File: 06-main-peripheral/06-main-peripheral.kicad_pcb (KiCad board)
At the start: 4 copper layers, 58.5 x 29.2 mm, 17 parts, among them J1 T4040014041000, J2 FH-41-15S-0.5SH-05_, J3 T4040014041000, J4 T4040014041000, Q1 DMN3018SSD-13, SW1 100SP1K1B25M1QEH-ND, U1 LM74700-Q1

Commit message: before revision from overlords
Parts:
- C1, C3, C4, C5: footprint Capacitor_SMD:C_0402_1005Metric_Pad0.74x0.62mm_HandSolder -> Capacitor_SMD:C_0603_1608Metric_Pad1.08x0.95mm_HandSolder
- R1, R2: footprint Resistor_SMD:R_0402_1005Metric_Pad0.72x0.64mm_HandSolder -> Resistor_SMD:R_0603_1608Metric_Pad0.98x0.95mm_HandSolder
- moved R1 3.24 mm to (150.5, 85.0)
- moved C4 1.84 mm to (141.8, 77.5)
- moved C3 0.59 mm to (177.1, 83.4)
- moved Q1 0.56 mm to (172.4, 81.6)
- moved R2 0.53 mm to (138.7, 78.5)
- moved C1 0.47 mm to (186.0, 83.3)
- moved C5 0.45 mm to (152.6, 79.1)
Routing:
- net LED_CONTROL: track 9.06 -> 12.0 mm
- net TX_N: track 13.1 -> 11.1 mm
- net USB_D_N: track 19.3 -> 17.7 mm
- net RX_N: track 11.6 -> 10.1 mm
- net GND: track 18.9 -> 20.4 mm
- net 5V: track 4.74 -> 6.01 mm
- added copper zone on B.Cu, net GND
- added copper zone on F.Cu, net GND

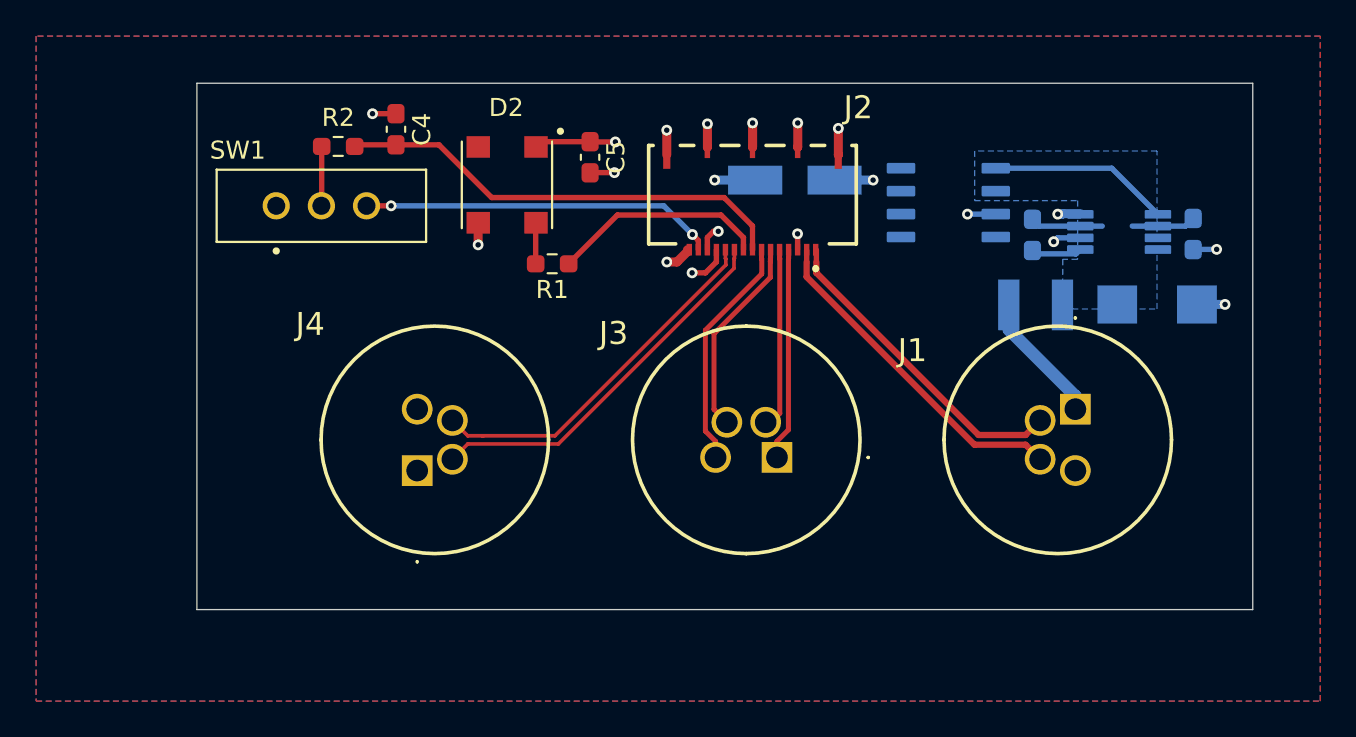
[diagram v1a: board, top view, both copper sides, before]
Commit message: added stitching vias
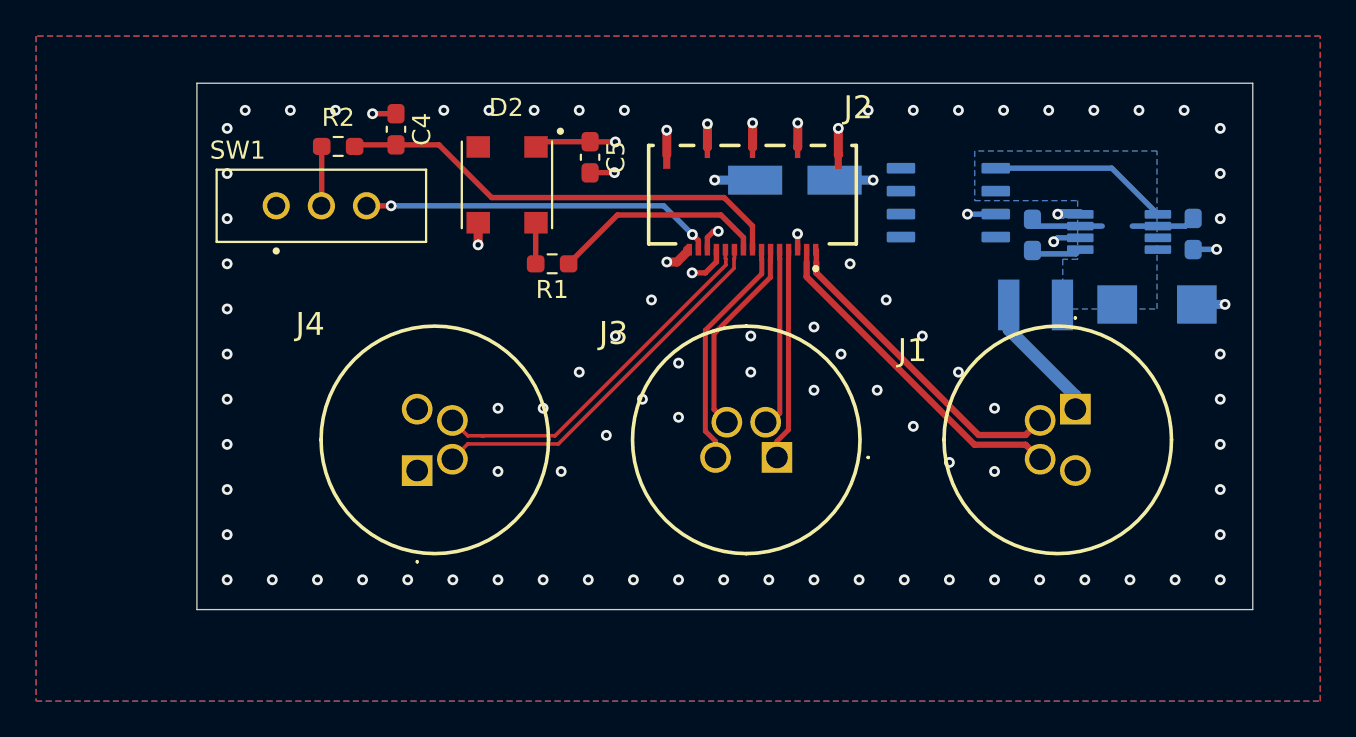
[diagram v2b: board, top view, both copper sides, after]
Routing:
- net GND: vias 14 -> 96

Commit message: added stitching vias correctly hopefully
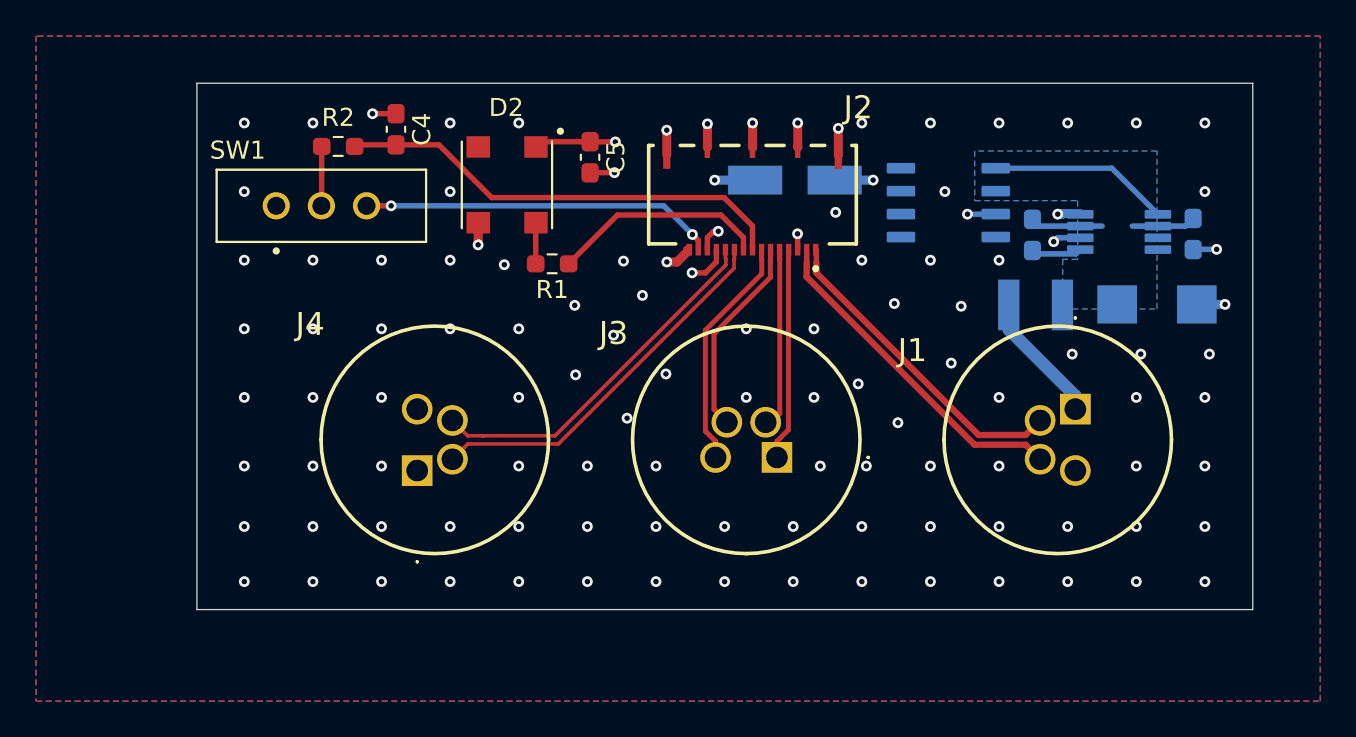
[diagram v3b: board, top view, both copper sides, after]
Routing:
- net GND: vias 96 -> 110

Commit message: fixed stitching vias
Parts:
- moved C2 0.21 mm to (164.2, 80.4)
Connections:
- J2 pad MP2: (no net) -> GND
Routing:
- net GND: vias 110 -> 108

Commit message: fixed stitching vias again
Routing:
- net GND: vias 108 -> 73

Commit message: Fixed mosfet routing
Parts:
- moved C2 0.25 mm to (163.9, 80.4), turned to 0 degrees
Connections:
- Q1 pad 1: Net-(Q1-G) -> Net-(D1-A2)
- Q1 pad 2: Net-(D1-A2) -> Net-(Q1-G)
- Q1 pad 3: USB_5V -> (no net)
- Q1 pad 7: (no net) -> USB_5V
- Q1 pad 8: (no net) -> USB_5V
- U1 pad 4: USB_5V -> GND
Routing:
- net Net-(Q1-G): track 9.48 -> 17.4 mm
- net USB_5V: track 6.39 -> 1.42 mm, vias 4 -> 3
- net GND: track 20.4 -> 21.7 mm, vias 73 -> 72
- added copper zone on B.Cu, net USB_5V
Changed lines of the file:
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@@
 		(capping no)
 		(filling no)
-		(zone_defaults)
 		(grid_origin 132.5 77.5)
 		(pcbplotparams
@@
 			(outputformat 1)
 			(mirror no)
-			(drillshape 1)
+			(drillshape 0)
 			(scaleselection 1)
 			(outputdirectory "")
@@
 	(footprint "Main_Peripheral:WCAP-ASLI_5X5.5_DXL_"
 		(layer "B.Cu")
-		(at 164.15 80.3656 180)
+		(at 163.9 80.3656)
 		(property "Reference" "C2"
 			(at -0.0086 3.7656 0)
@@
 		(duplicate_pad_numbers_are_jumpers no)
 		(fp_line
-			(start 2.75 1.7)
-			(end 2.75 1.1)
+			(start -2.75 -2.75)
+			(end -2.75 -1.1)
 			(stroke
 				(width 0.2)
@@
 		)
 		(fp_line
-			(start 2.75 -1.7)
-			(end 2.75 -1.1)
+			(start -2.75 -2.75)
+			(end 1.7 -2.75)
 			(stroke
 				(width 0.2)
@@
 		)
 		(fp_line
-			(start 1.7 2.75)
-			(end 2.75 1.7)
+			(start -2.75 2.75)
+			(end -2.75 1.1)
 			(stroke
 				(width 0.2)
@@
 		)
 		(fp_line
-			(start 1.7 -2.75)
-			(end 2.75 -1.7)
+			(start -2.75 2.75)
+			(end 1.7 2.75)
 			(stroke
 				(width 0.2)
@@
 		)
 		(fp_line
-			(start -2.75 2.75)
-			(end 1.7 2.75)
+			(start 1.7 -2.75)
+			(end 2.75 -1.7)
 			(stroke
 				(width 0.2)
@@
 		)
 		(fp_line
-			(start -2.75 2.75)
-			(end -2.75 1.1)
+			(start 1.7 2.75)
+			(end 2.75 1.7)
 			(stroke
 				(width 0.2)
@@
 		)
 		(fp_line
-			(start -2.75 -2.75)
-			(end 1.7 -2.75)
+			(start 2.75 -1.7)
+			(end 2.75 -1.1)
 			(stroke
 				(width 0.2)
@@
 		)
 		(fp_line
-			(start -2.75 -2.75)
-			(end -2.75 -1.1)
+			(start 2.75 1.7)
+			(end 2.75 1.1)
 			(stroke
 				(width 0.2)
@@
 		)
 		(fp_line
-			(start 2.65 1.65)
-			(end 1.65 2.65)
+			(start -2.65 -2.65)
+			(end 1.65 -2.65)
 			(stroke
 				(width 0.1)
@@
 		)
 		(fp_line
-			(start 2.65 -1.65)
-			(end 2.65 1.65)
+			(start -2.65 2.65)
+			(end -2.65 -2.65)
 			(stroke
 				(width 0.1)
@@
 		)
 		(fp_line
-			(start 1.65 2.65)
-			(end -2.65 2.65)
+			(start 1.65 -2.65)
+			(end 2.65 -1.65)
 			(stroke
 				(width 0.1)
@@
 		)
 		(fp_line
-			(start 1.65 -2.65)
-			(end 2.65 -1.65)
+			(start 1.65 2.65)
+			(end -2.65 2.65)
 			(stroke
 				(width 0.1)
@@
 		)
 		(fp_line
-			(start -2.65 2.65)
-			(end -2.65 -2.65)
+			(start 2.65 -1.65)
+			(end 2.65 1.65)
 			(stroke
 				(width 0.1)
@@
 		)
 		(fp_line
-			(start -2.65 -2.65)
-			(end 1.65 -2.65)
+			(start 2.65 1.65)
+			(end 1.65 2.65)
 			(stroke
 				(width 0.1)
@@
 		)
 		(pad "1" smd rect
-			(at 2.2 0 180)
+			(at 2.2 0)
 			(size 3 1.6)
 			(layers "B.Cu" "B.Mask" "B.Paste")
@@
 		)
 		(pad "2" smd rect
-			(at -2.2 0 180)
+			(at -2.2 0)
 			(size 3 1.6)
 			(layers "B.Cu" "B.Mask" "B.Paste")
@@
 			(unit
 				(name "A")
-				(pins "1" "3" "2")
+				(pins "2" "7" "1")
 			)
 		)
@@
 			(layers "B.Cu" "B.Mask" "B.Paste")
 			(roundrect_rratio 0.125)
-			(net "Net-(Q1-G)")
-			(pinfunction "G_1")
-			(pintype "input")
+			(net "Net-(D1-A2)")
+			(pinfunction "S_1")
+			(pintype "passive")
 			(solder_mask_margin 0.102)
 		)
@@
 			(layers "B.Cu" "B.Mask" "B.Paste")
 			(roundrect_rratio 0.125)
-			(net "Net-(D1-A2)")
-			(pinfunction "S_2")
-			(pintype "passive")
+			(net "Net-(Q1-G)")
+			(pinfunction "G_2")
+			(pintype "input")
 			(solder_mask_margin 0.102)
 		)
@@
 			(layers "B.Cu" "B.Mask" "B.Paste")
 			(roundrect_rratio 0.125)
-			(net "USB_5V")
-			(pinfunction "D_3")
-			(pintype "passive")
 			(solder_mask_margin 0.102)
 		)
@@
 			(layers "B.Cu" "B.Mask" "B.Paste")
 			(roundrect_rratio 0.125)
+			(net "USB_5V")
+			(pinfunction "D_7")
+			(pintype "passive")
 			(solder_mask_margin 0.102)
 		)
@@
 			(layers "B.Cu" "B.Mask" "B.Paste")
 			(roundrect_rratio 0.125)
+			(net "USB_5V")
 			(solder_mask_margin 0.102)
 		)
@@
 			(layers "B.Cu" "B.Mask" "B.Paste")
 			(roundrect_rratio 0.125)
-			(net "USB_5V")
+			(net "GND")
 			(pinfunction "CATHODE_4")
 			(pintype "input")
@@
 	)
 	(via
+		(at 159.8086 80.3656)
+		(size 0.6)
+		(drill 0.3)
+		(layers "F.Cu" "B.Cu")
+		(free yes)
+		(net "GND")
+	)
+	(via
 		(at 137.25 77.2)
 		(size 0.6)
@@
 	)
 	(via
-		(at 168.4836 80.3656)
-		(size 0.6)
-		(drill 0.3)
-		(layers "F.Cu" "B.Cu")
-		(net "GND")
-	)
-	(via
 		(at 156.25 102.6)
 		(size 0.6)
@@
 	)
 	(via
-		(at 166.2 82.15)
-		(size 0.6)
-		(drill 0.3)
-		(layers "F.Cu" "B.Cu")
-		(free yes)
-		(net "GND")
-	)
-	(via
 		(at 153.95 79.95)
 		(size 0.6)
@@
 	)
 	(via
-		(at 172.25 81)
-		(size 0.6)
-		(drill 0.3)
-		(layers "F.Cu" "B.Cu")
-		(free yes)
-		(net "GND")
-	)
-	(via
 		(at 141.05 88.6)
 		(size 0.6)
@@
 	)
 	(via
+		(at 178.5 82.25)
+		(size 0.6)
+		(drill 0.3)
+		(layers "F.Cu" "B.Cu")
+		(free yes)
+		(net "GND")
+	)
+	(via
 		(at 163.85 102.6)
 		(size 0.6)
@@
 	)
 	(segment
+		(start 159.8086 80.3656)
+		(end 161.95 80.3656)
+		(width 0.5)
+		(layer "B.Cu")
+		(net "GND")
+	)
+	(segment
 		(start 187.3 84.2)
 		(end 186.0125 84.2)
@@
 	)
 	(segment
+		(start 178.5 82.25)
+		(end 178.75 82.25)
+		(width 0.5)
+		(layer "B.Cu")
+		(net "GND")
+	)
+	(segment
 		(start 179.7431 83.567)
 		(end 179.7483 83.5618)
@@
 	)
 	(segment
-		(start 168.4836 80.3656)
-		(end 166.35 80.3656)
+		(start 178.75 82.25)
+		(end 178.7782 82.2218)
 		(width 0.5)
 		(layer "B.Cu")
@@
 	)
 	(segment
+		(start 178.7782 82.2218)
+		(end 179.7483 82.2218)
+		(width 0.5)
+		(layer "B.Cu")
+		(net "GND")
+	)
+	(segment
 		(start 146.606354 94.5235)
 		(end 146.706791 94.5235)
@@
 	)
 	(via
-		(at 159.8086 80.3656)
+		(at 168.35 79.9)
 		(size 0.6)
 		(drill 0.3)
@@
 	)
 	(via
-		(at 173.5 82.25)
+		(at 168.35 80.85)
 		(size 0.6)
 		(drill 0.3)
@@
 		(net "USB_5V")
 	)
-	(via
-		(at 178.5 82.25)
-		(size 0.6)
-		(drill 0.3)
-		(layers "F.Cu" "B.Cu")
-		(free yes)
-		(net "USB_5V")
-	)
 	(segment
-		(start 159.8086 80.3656)
-		(end 161.95 80.3656)
-		(width 0.5)
+		(start 173.7 79.1)
+		(end 173.7 80.5)
+		(width 0.3)
 		(layer "B.Cu")
-		(net "USB_5V")
+		(net "Net-(Q1-G)")
 	)
 	(segment
-		(start 175.0637 82.25)
-		(end 175.0675 82.2462)
+		(start 174.3 78.5)
+		(end 173.7 79.1)
 		(width 0.3)
 		(layer "B.Cu")
-		(net "USB_5V")
+		(net "Net-(Q1-G)")
 	)
 	(segment
-		(start 173.5 82.25)
-		(end 175.0637 82.25)
+		(start 184.3 82.0101)
+		(end 184.3 78.9)
 		(width 0.3)
 		(layer "B.Cu")
-		(net "USB_5V")
+		(net "Net-(Q1-G)")
 	)
 	(segment
-		(start 178.5 82.25)
-		(end 178.75 82.25)
-		(width 0.5)
+		(start 173.7 80.5)
+		(end 174.1762 80.9762)
+		(width 0.3)
 		(layer "B.Cu")
-		(net "USB_5V")
+		(net "Net-(Q1-G)")
 	)
 	(segment
-		(start 178.75 82.25)
-		(end 178.7782 82.2218)
-		(width 0.5)
+		(start 184.3 78.9)
+		(end 183.9 78.5)
+		(width 0.3)
 		(layer "B.Cu")
-		(net "USB_5V")
+		(net "Net-(Q1-G)")
 	)
 	(segment
-		(start 178.7782 82.2218)
-		(end 179.7483 82.2218)
-		(width 0.5)
+		(start 174.1762 80.9762)
+		(end 175.0675 80.9762)
+		(width 0.3)
 		(layer "B.Cu")
-		(net "USB_5V")
+		(net "Net-(Q1-G)")
 	)
 	(segment
 		(start 184.0483 82.2618)
-		(end 181.4927 79.7062)
+		(end 184.3 82.0101)
 		(width 0.3)
 		(layer "B.Cu")
@@
 	)
 	(segment
-		(start 181.4927 79.7062)
-		(end 175.6314 79.7062)
+		(start 183.9 78.5)
+		(end 174.3 78.5)
 		(width 0.3)
 		(layer "B.Cu")
@@
 		(priority 3)
 		(connect_pads
-			(clearance 0.2)
+			(clearance 0.3)
 		)
 		(min_thickness 0.25)
@@
 	)
 	(zone
+		(net "USB_5V")
+		(layer "B.Cu")
+		(hatch edge 0.5)
+		(priority 5)
+		(connect_pads yes
+			(clearance 0.2)
+		)
+		(min_thickness 0.25)
+		(fill yes
+			(thermal_gap 0.5)
+			(thermal_bridge_width 0.5)
+			(island_removal_mode 0)
+		)
+		(polygon
+			(pts
+				(xy 164.35 79.2656) (xy 164.35 81.45) (xy 170.85 81.4) (xy 170.85 79.2) (xy 170.85 79.25)
+			)
+		)
+	)
+	(zone
 		(net "Net-(D1-A2)")
 		(layer "B.Cu")
 		(hatch edge 0.5)
 		(priority 4)
-		(connect_pads
+		(connect_pads yes
 			(clearance 0.5)
 		)
